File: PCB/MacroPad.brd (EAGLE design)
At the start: 76.2 x 76.2 mm, 42 parts, among them SW00 SWITCH-SMD-EVQP-P2602W, SW01 KEYSWITCH-PLAIN-MX-1U, SW02 KEYSWITCH-PLAIN-MX-1U, SW03 KEYSWITCH-PLAIN-MX-1U, SW04 KEYSWITCH-PLAIN-MX-1U, SW05 KEYSWITCH-PLAIN-MX-1U, SW06 KEYSWITCH-PLAIN-MX-1U, SW07 KEYSWITCH-PLAIN-MX-1U, SW08 KEYSWITCH-PLAIN-MX-1U, SW09 KEYSWITCH-PLAIN-MX-1U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

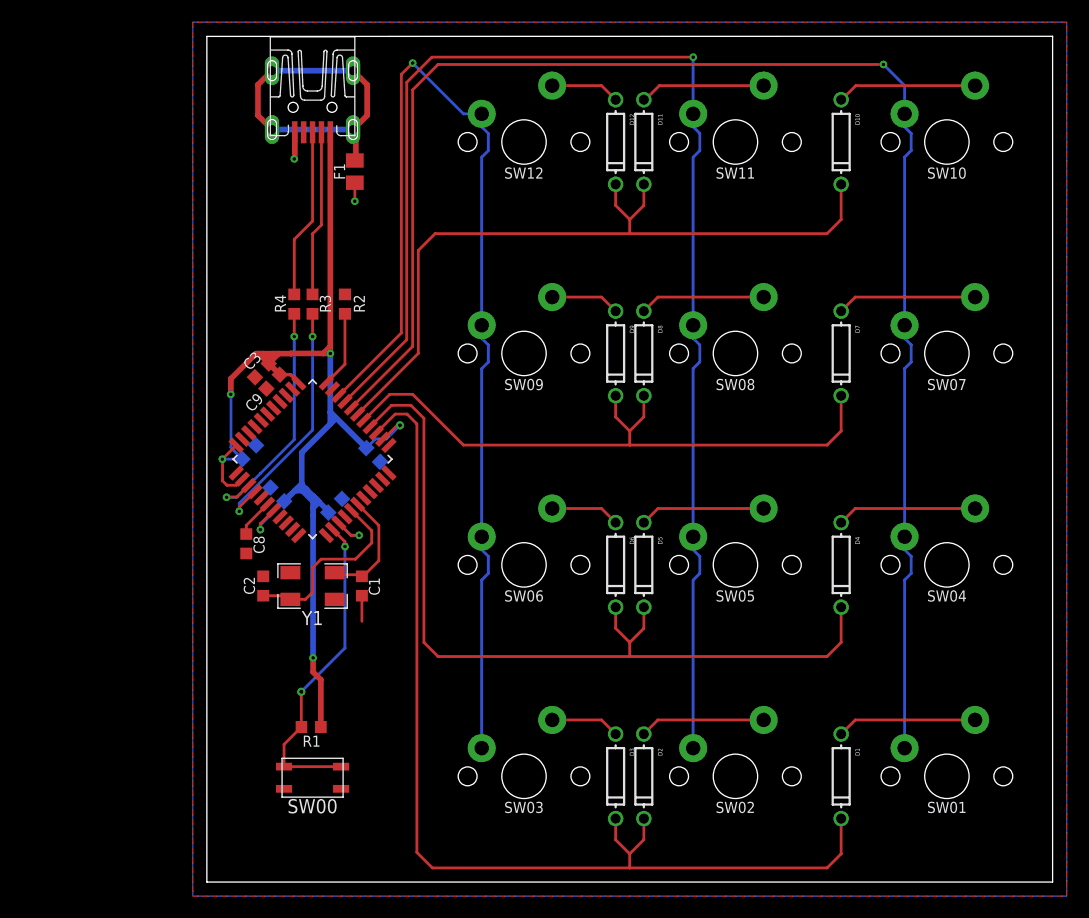
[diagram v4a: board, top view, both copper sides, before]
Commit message: Reroute columns to avoid vias
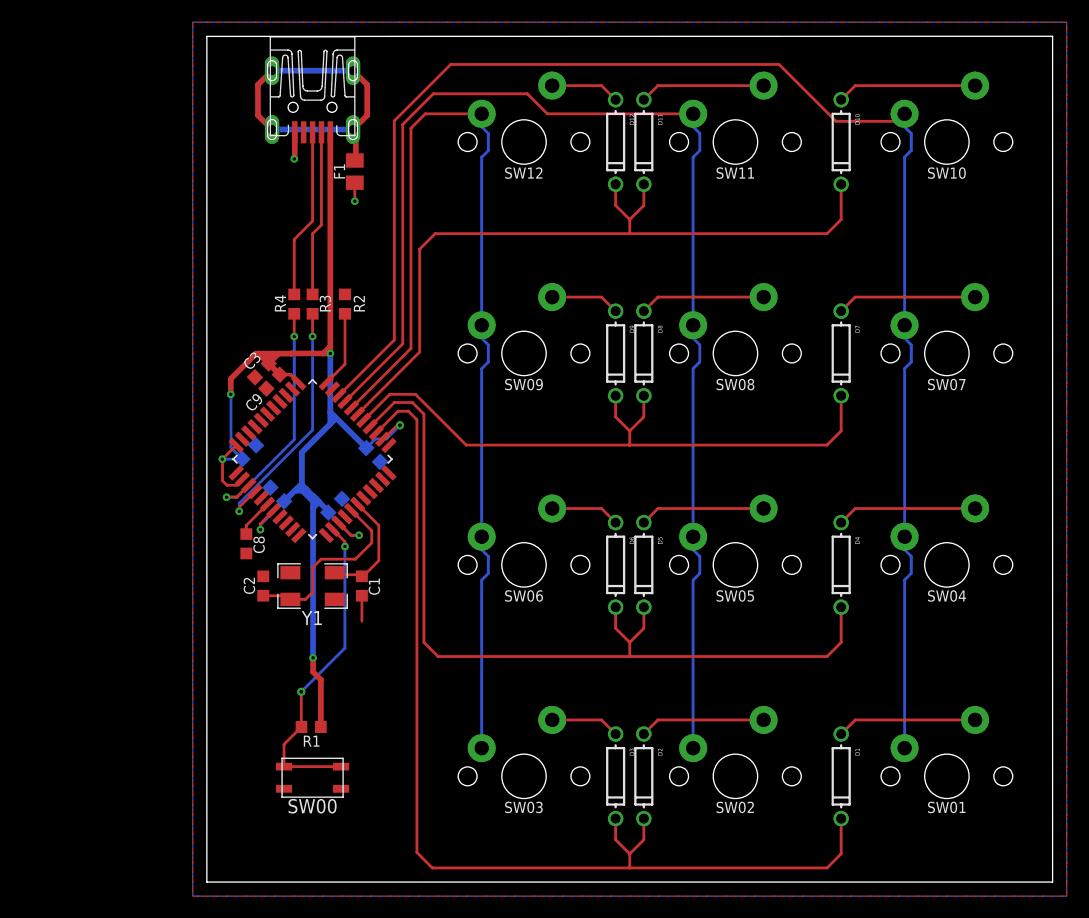
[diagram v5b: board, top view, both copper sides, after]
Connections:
- net N$10: now also U1.31; no longer U1.29
- net N$16: now also U1.29; no longer U1.31
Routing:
- net N$40: track 121.5 -> 113.8 mm, vias 1 -> 0
- net N$16: track 99.4 -> 93.0 mm, vias 1 -> 0
- net N$10: track 138.2 -> 135.9 mm, vias 1 -> 0
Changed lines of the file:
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@@
 <wire x1="63.461" y1="27.802075" x2="62.865" y2="27.206075" width="0.254" layer="16"/>
 <wire x1="62.865" y1="27.206075" x2="62.865" y2="12.065" width="0.254" layer="16"/>
-<wire x1="18.542" y1="71.374" x2="20.828" y2="73.66" width="0.254" layer="1"/>
-<wire x1="20.828" y1="73.66" x2="60.96" y2="73.66" width="0.254" layer="1"/>
-<via x="60.96" y="73.66" extent="1-16" drill="0.3048"/>
-<wire x1="60.96" y1="73.66" x2="62.865" y2="71.755" width="0.254" layer="16"/>
-<wire x1="62.865" y1="71.755" x2="62.865" y2="69.215" width="0.254" layer="16"/>
-<wire x1="18.542" y1="48.26" x2="18.542" y2="71.374" width="0.254" layer="1"/>
-<contactref element="U1" pad="29"/>
-<wire x1="13.027296875" y1="42.71585" x2="13.027296875" y2="42.745296875" width="0.254" layer="1"/>
-<wire x1="13.027296875" y1="42.745296875" x2="18.542" y2="48.26" width="0.254" layer="1"/>
+<contactref element="U1" pad="31"/>
+<wire x1="16.891" y1="48.842575" x2="11.8957875" y2="43.8473625" width="0.254" layer="1"/>
+<wire x1="16.891" y1="68.58" x2="21.971" y2="73.66" width="0.254" layer="1"/>
+<wire x1="21.971" y1="73.66" x2="51.562" y2="73.66" width="0.254" layer="1"/>
+<wire x1="62.191" y1="68.541" x2="62.865" y2="69.215" width="0.254" layer="1"/>
+<wire x1="56.681" y1="68.541" x2="62.191" y2="68.541" width="0.254" layer="1"/>
+<wire x1="16.891" y1="48.842575" x2="16.891" y2="68.58" width="0.254" layer="1"/>
+<wire x1="51.562" y1="73.66" x2="56.681" y2="68.541" width="0.254" layer="1"/>
 </signal>
 <signal name="N$12">
@@
 </signal>
 <signal name="N$14">
-<wire x1="18.034" y1="42.164" x2="18.923" y2="41.275" width="0.254" layer="1"/>
+<wire x1="18.161" y1="42.418" x2="18.923" y2="41.656" width="0.254" layer="1"/>
 <contactref element="D1" pad="C"/>
 <contactref element="D2" pad="C"/>
@@
 <wire x1="55.88" y1="1.27" x2="57.15" y2="2.54" width="0.254" layer="1"/>
 <wire x1="57.15" y1="2.54" x2="57.15" y2="5.715" width="0.254" layer="1"/>
-<wire x1="18.923" y1="41.275" x2="18.923" y2="2.667" width="0.254" layer="1"/>
+<wire x1="18.923" y1="41.656" x2="18.923" y2="2.667" width="0.254" layer="1"/>
 <wire x1="36.83" y1="5.715" x2="36.83" y2="3.81" width="0.254" layer="1"/>
 <wire x1="36.83" y1="3.81" x2="38.1" y2="2.54" width="0.254" layer="1"/>
@@
 <wire x1="38.1" y1="2.54" x2="38.1" y2="1.27" width="0.254" layer="1"/>
 <contactref element="U1" pad="25"/>
-<wire x1="15.2723625" y1="40.4707875" x2="16.965575" y2="42.164" width="0.254" layer="1"/>
-<wire x1="16.965575" y1="42.164" x2="18.034" y2="42.164" width="0.254" layer="1"/>
+<wire x1="15.2723625" y1="40.4707875" x2="17.219575" y2="42.418" width="0.254" layer="1"/>
+<wire x1="17.219575" y1="42.418" x2="18.161" y2="42.418" width="0.254" layer="1"/>
 </signal>
 <signal name="N$15">
@@
 <wire x1="25.361" y1="27.802075" x2="24.765" y2="27.206075" width="0.254" layer="16"/>
 <wire x1="24.765" y1="27.206075" x2="24.765" y2="12.065" width="0.254" layer="16"/>
-<wire x1="11.8957875" y1="43.8473625" x2="17.526" y2="49.477575" width="0.254" layer="1"/>
-<wire x1="17.526" y1="49.477575" x2="17.526" y2="72.771" width="0.254" layer="1"/>
-<wire x1="17.526" y1="72.771" x2="18.542" y2="73.787" width="0.254" layer="1"/>
-<via x="18.542" y="73.787" extent="1-16" drill="0.3048"/>
-<wire x1="18.542" y1="73.787" x2="23.114" y2="69.215" width="0.254" layer="16"/>
-<wire x1="23.114" y1="69.215" x2="24.765" y2="69.215" width="0.254" layer="16"/>
-<contactref element="U1" pad="31"/>
+<contactref element="U1" pad="29"/>
+<wire x1="13.027296875" y1="42.71585" x2="18.3896" y2="48.078153125" width="0.254" layer="1"/>
+<wire x1="18.3896" y1="67.9196" x2="19.685" y2="69.215" width="0.254" layer="1"/>
+<wire x1="19.685" y1="69.215" x2="24.765" y2="69.215" width="0.254" layer="1"/>
+<wire x1="18.3896" y1="48.078153125" x2="18.3896" y2="67.9196" width="0.254" layer="1"/>
 </signal>
 <signal name="N$18">
@@
 <wire x1="55.88" y1="20.32" x2="57.15" y2="21.59" width="0.254" layer="1"/>
 <wire x1="57.15" y1="21.59" x2="57.15" y2="24.765" width="0.254" layer="1"/>
-<wire x1="19.558" y1="41.783" x2="19.558" y2="21.59" width="0.254" layer="1"/>
+<wire x1="19.558" y1="42.164" x2="19.558" y2="21.59" width="0.254" layer="1"/>
 <wire x1="36.83" y1="24.765" x2="36.83" y2="22.86" width="0.254" layer="1"/>
 <wire x1="36.83" y1="22.86" x2="38.1" y2="21.59" width="0.254" layer="1"/>
@@
 <wire x1="39.37" y1="22.86" x2="38.1" y2="21.59" width="0.254" layer="1"/>
 <contactref element="U1" pad="26"/>
-<wire x1="18.3896" y1="42.9514" x2="16.639425" y2="42.9514" width="0.254" layer="1"/>
-<wire x1="16.639425" y1="42.9514" x2="14.7155875" y2="41.0275625" width="0.254" layer="1"/>
-<wire x1="19.558" y1="41.783" x2="18.3896" y2="42.9514" width="0.254" layer="1"/>
+<wire x1="18.5166" y1="43.2054" x2="16.893425" y2="43.2054" width="0.254" layer="1"/>
+<wire x1="16.893425" y1="43.2054" x2="14.7155875" y2="41.0275625" width="0.254" layer="1"/>
+<wire x1="19.558" y1="42.164" x2="18.5166" y2="43.2054" width="0.254" layer="1"/>
 <wire x1="19.558" y1="21.59" x2="20.828" y2="20.32" width="0.254" layer="1"/>
 <wire x1="20.828" y1="20.32" x2="38.1" y2="20.32" width="0.254" layer="1"/>
@@
 <contactref element="D8" pad="C"/>
 <contactref element="D7" pad="C"/>
-<wire x1="23.114" y1="39.37" x2="38.1" y2="39.37" width="0.254" layer="1"/>
+<wire x1="23.368" y1="39.37" x2="38.1" y2="39.37" width="0.254" layer="1"/>
 <wire x1="38.1" y1="39.37" x2="55.88" y2="39.37" width="0.254" layer="1"/>
 <wire x1="55.88" y1="39.37" x2="57.15" y2="40.64" width="0.254" layer="1"/>
@@
 <contactref element="U1" pad="27"/>
 <wire x1="14.14085" y1="41.602296875" x2="16.480553125" y2="43.942" width="0.254" layer="1"/>
-<wire x1="16.480553125" y1="43.942" x2="18.542" y2="43.942" width="0.254" layer="1"/>
-<wire x1="18.542" y1="43.942" x2="23.114" y2="39.37" width="0.254" layer="1"/>
+<wire x1="16.480553125" y1="43.942" x2="18.796" y2="43.942" width="0.254" layer="1"/>
+<wire x1="18.796" y1="43.942" x2="23.368" y2="39.37" width="0.254" layer="1"/>
 </signal>
 <signal name="N$33">
@@
 <signal name="N$36">
 <contactref element="SW10" pad="MX2"/>
-<wire x1="69.215" y1="71.755" x2="58.4696" y2="71.755" width="0.254" layer="1"/>
-<wire x1="57.15" y1="70.4354" x2="58.4696" y2="71.755" width="0.254" layer="1"/>
 <contactref element="D10" pad="A"/>
-<wire x1="57.15" y1="70.485" x2="57.15" y2="70.4354" width="0" layer="19" extent="1-1"/>
+<wire x1="58.42" y1="71.755" x2="57.15" y2="70.485" width="0.254" layer="1"/>
+<wire x1="69.215" y1="71.755" x2="58.42" y2="71.755" width="0.254" layer="1"/>
 </signal>
 <signal name="N$38">
 <wire x1="55.88" y1="58.42" x2="57.15" y2="59.69" width="0.254" layer="1"/>
-<wire x1="19.05" y1="47.625" x2="19.05" y2="56.896" width="0.254" layer="1"/>
-<wire x1="19.05" y1="56.896" x2="20.574" y2="58.42" width="0.254" layer="1"/>
+<wire x1="19.177" y1="47.752" x2="19.177" y2="57.023" width="0.254" layer="1"/>
+<wire x1="19.177" y1="57.023" x2="20.574" y2="58.42" width="0.254" layer="1"/>
 <contactref element="D10" pad="C"/>
 <contactref element="D11" pad="C"/>
@@
 <wire x1="20.574" y1="58.42" x2="38.1" y2="58.42" width="0.254" layer="1"/>
 <contactref element="U1" pad="28"/>
-<wire x1="13.584075" y1="42.159075" x2="19.05" y2="47.625" width="0.254" layer="1"/>
+<wire x1="13.584075" y1="42.159075" x2="19.177" y2="47.752" width="0.254" layer="1"/>
 </signal>
 <signal name="N$39">
 <contactref element="SW11" pad="MX2"/>
-<wire x1="39.37" y1="70.358" x2="40.767" y2="71.755" width="0.254" layer="1"/>
-<wire x1="40.767" y1="71.755" x2="50.165" y2="71.755" width="0.254" layer="1"/>
 <contactref element="D11" pad="A"/>
-<wire x1="39.37" y1="70.485" x2="39.37" y2="70.358" width="0" layer="19" extent="1-1"/>
+<wire x1="40.64" y1="71.755" x2="39.37" y2="70.485" width="0.254" layer="1"/>
+<wire x1="50.165" y1="71.755" x2="40.64" y2="71.755" width="0.254" layer="1"/>
 </signal>
 <signal name="N$40">
@@
 <wire x1="44.411" y1="27.802075" x2="43.815" y2="27.206075" width="0.254" layer="16"/>
 <wire x1="43.815" y1="27.206075" x2="43.815" y2="12.065" width="0.254" layer="16"/>
-<wire x1="18.0086" y1="72.0503375" x2="20.2786625" y2="74.3204" width="0.254" layer="1"/>
-<via x="43.815" y="74.3176" extent="1-16" drill="0.3048"/>
-<wire x1="43.815" y1="74.3176" x2="43.815" y2="69.215" width="0.254" layer="16"/>
-<wire x1="18.0086" y1="48.8696" x2="18.0086" y2="72.0503375" width="0.254" layer="1"/>
-<wire x1="20.2786625" y1="74.3204" x2="43.8122" y2="74.3204" width="0.254" layer="1"/>
-<wire x1="43.8122" y1="74.3204" x2="43.815" y2="74.3176" width="0.254" layer="1"/>
 <contactref element="U1" pad="30"/>
 <wire x1="12.4525625" y1="43.2905875" x2="12.4525625" y2="43.3135625" width="0.254" layer="1"/>
-<wire x1="12.4525625" y1="43.3135625" x2="18.0086" y2="48.8696" width="0.254" layer="1"/>
+<wire x1="17.653" y1="48.491025" x2="12.4525625" y2="43.2905875" width="0.254" layer="1"/>
+<wire x1="17.653" y1="48.491025" x2="17.653" y2="68.2657375" width="0.254" layer="1"/>
+<wire x1="17.653" y1="68.2657375" x2="20.4056625" y2="71.0184" width="0.254" layer="1"/>
+<wire x1="20.4056625" y1="71.0184" x2="28.87786875" y2="71.0184" width="0.254" layer="1"/>
+<wire x1="28.87786875" y1="71.0184" x2="30.68126875" y2="69.215" width="0.254" layer="1"/>
+<wire x1="30.68126875" y1="69.215" x2="43.815" y2="69.215" width="0.254" layer="1"/>
 </signal>
 <signal name="N$42">
